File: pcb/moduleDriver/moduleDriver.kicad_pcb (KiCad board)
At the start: 2 copper layers, 70 x 80 mm, 37 parts, among them J1 MOTOR, J10 Sensor, J11 Power, J12 Power, J13 Power, J2 MOTOR, J3 MOTOR, J4 MOTOR, J5 IDC, J6 IDC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

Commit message: Simple PCB fixes
- Change C2, C3, C5, C6 all to 1uF
- Delete R4
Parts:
- C2, C3, C5, C6: value 0.1uF -> 1uF
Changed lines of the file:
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@@
       (effects (font (size 1 1) (thickness 0.15)))
     )
-    (fp_text value "0.1uF" (at 0 1.43) (layer "F.Fab")
+    (fp_text value "1uF" (at 0 1.43) (layer "F.Fab")
       (effects (font (size 1 1) (thickness 0.15)))
     )
@@
       (effects (font (size 1 1) (thickness 0.15)))
     )
-    (fp_text value "0.1uF" (at 0 1.43) (layer "F.Fab")
+    (fp_text value "1uF" (at 0 1.43) (layer "F.Fab")
       (effects (font (size 1 1) (thickness 0.15)))
     )
@@
       (effects (font (size 1 1) (thickness 0.15)))
     )
-    (fp_text value "0.1uF" (at 0 1.43 90) (layer "F.Fab")
+    (fp_text value "1uF" (at 0 1.43 90) (layer "F.Fab")
       (effects (font (size 1 1) (thickness 0.15)))
     )
@@
       (effects (font (size 1 1) (thickness 0.15)))
     )
-    (fp_text value "0.1uF" (at 0 1.43 90) (layer "F.Fab")
-      (effects (font (size 1 1) (thickness 0.15)))
-    )
+    (fp_text value "1uF" (at 0 1.43 90) (layer "F.Fab")
+      (effects (font (size 1 1) (thickness 0.15)))
+    )

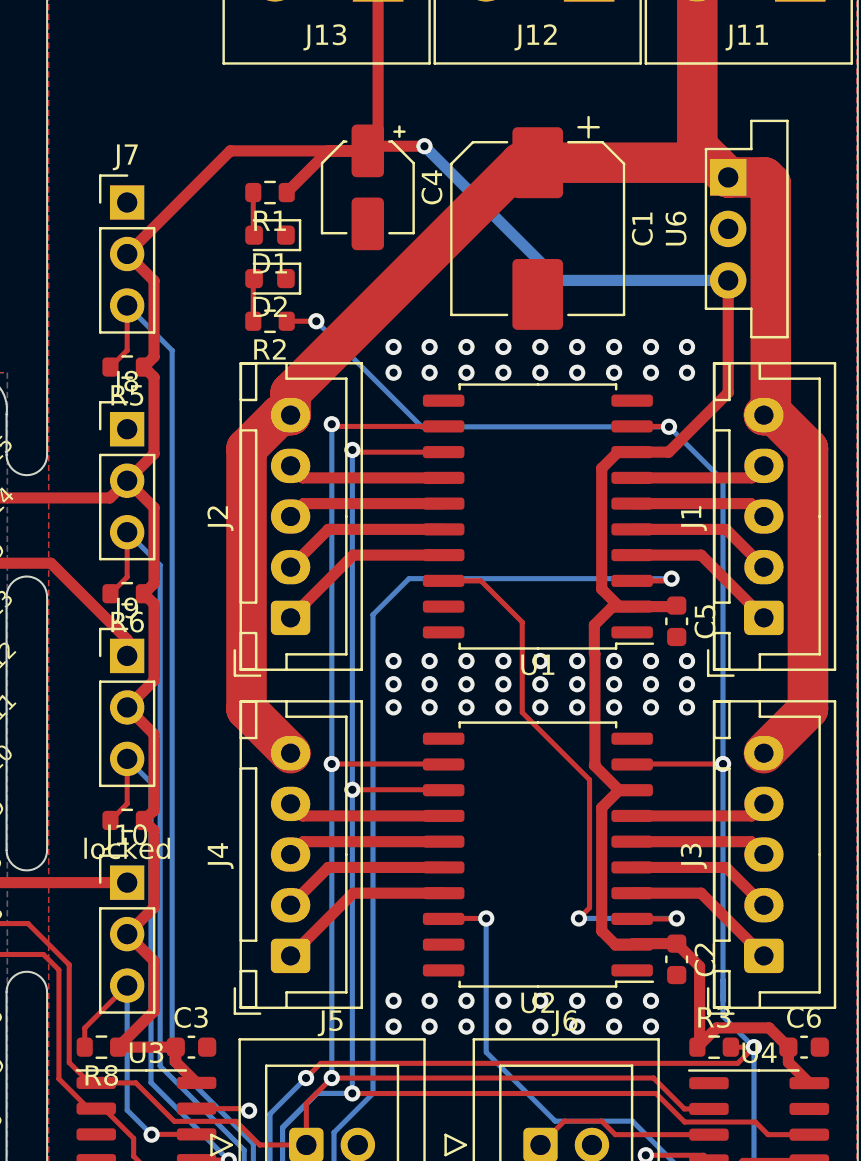
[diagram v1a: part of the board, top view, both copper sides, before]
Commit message: Added 12v led
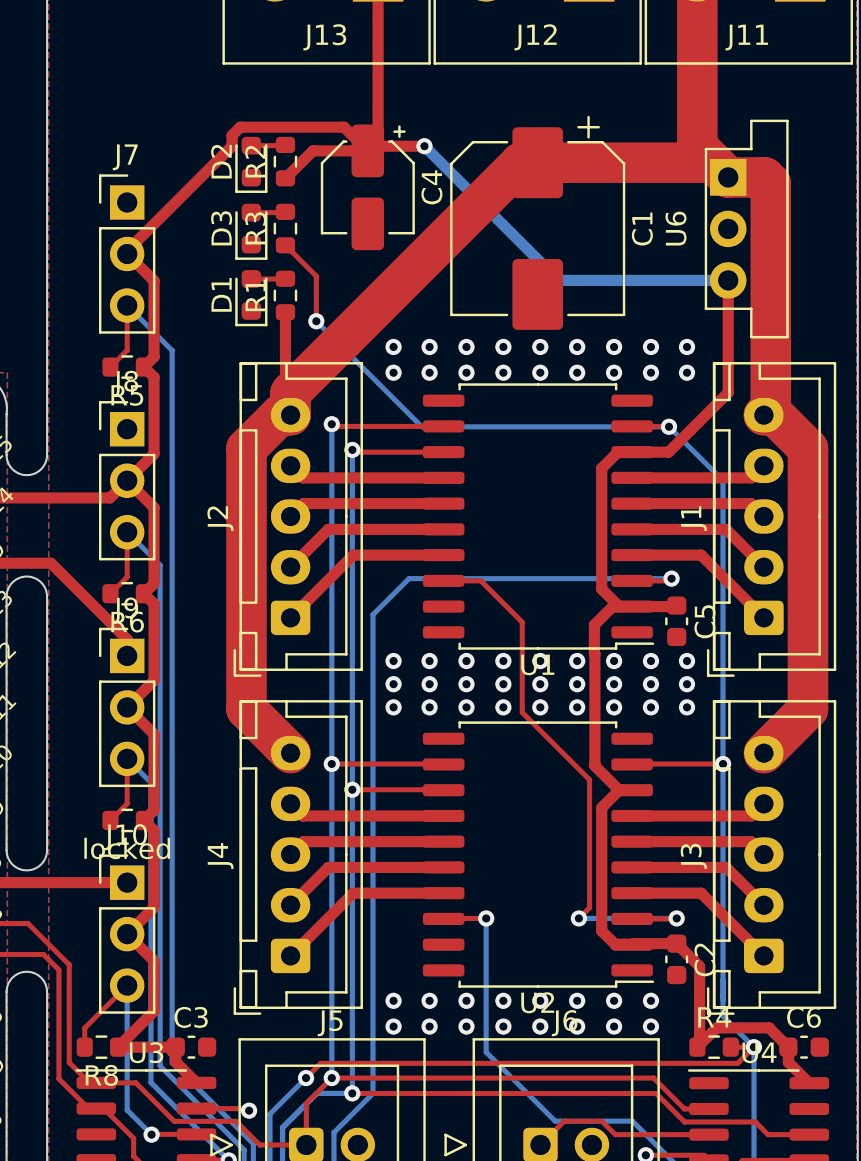
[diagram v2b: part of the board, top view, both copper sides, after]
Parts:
- added D1: LED, LED_SMD:LED_0603_1608Metric, F.Cu at (110.1, 72.1)
- added R1: 220R, Resistor_SMD:R_0603_1608Metric, F.Cu at (111.8, 72.1)
- moved R3 4.64 mm to (111.8, 68.8), turned to 90 degrees
- moved D2 3.74 mm to (110.1, 65.5), turned to 90 degrees
- moved D3 2.63 mm to (110.1, 68.8), turned to 90 degrees
- moved R2 1.70 mm to (111.8, 65.5), turned to 90 degrees
- renumbered D1 to D2, D2 to D3, R1 to R2, R2 to R3, R3 to R4
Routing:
- net +12V: track 94.7 -> 99.9 mm
- net /PWR_ENABLE_IN: track 125.8 -> 128.7 mm
- net Net-(D1-Pad2): track 0.00 -> 1.69 mm
- net +5V: track 248.5 -> 249.6 mm

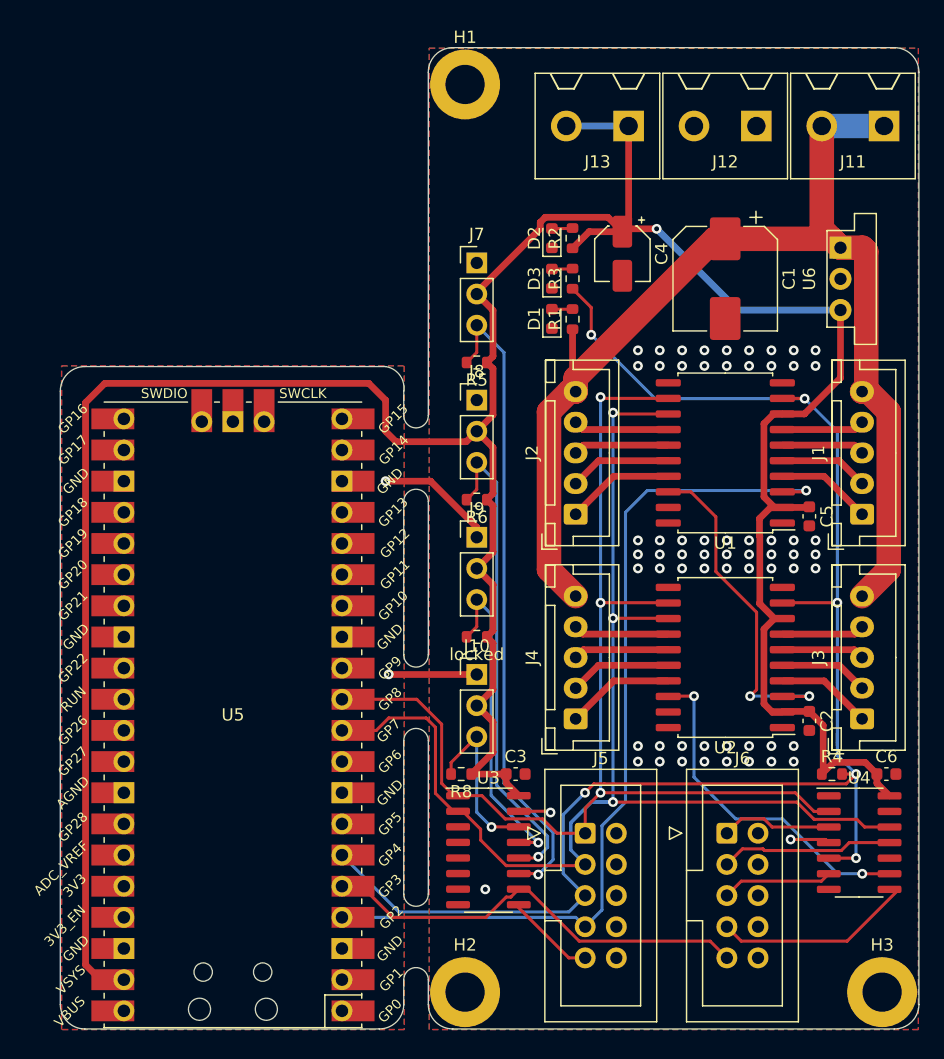
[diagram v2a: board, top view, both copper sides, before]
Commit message: Inital layout for voltage level translation
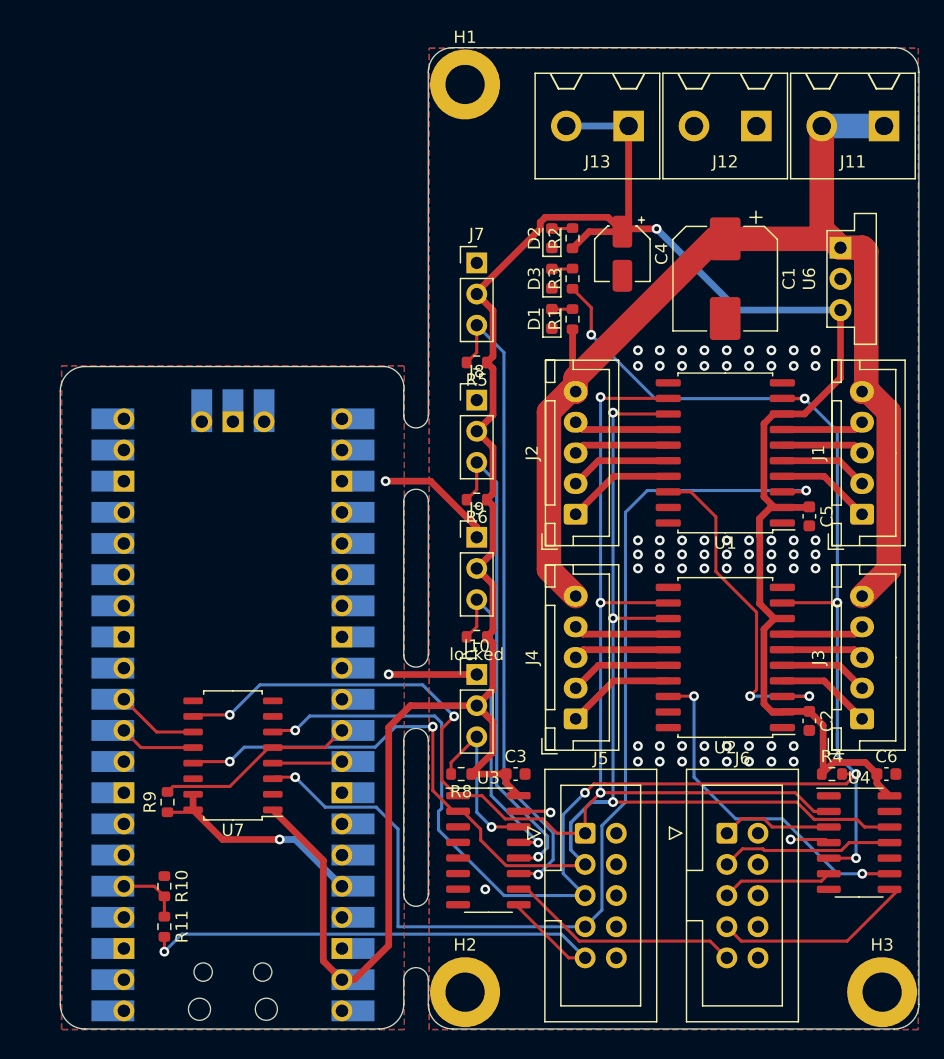
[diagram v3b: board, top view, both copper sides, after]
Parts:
- added R10: 2k, Resistor_SMD:R_0603_1608Metric, F.Cu at (78.5, 118.4)
- added R11: 1k, Resistor_SMD:R_0603_1608Metric, F.Cu at (78.5, 121.7)
- added R9: 5k, Resistor_SMD:R_0603_1608Metric, F.Cu at (78.7, 111.5)
- added U7: HEF4104B, Package_SO:SOIC-16_4.55x10.3mm_P1.27mm, F.Cu at (84.1, 107.7)
- U5: moved to B.Cu
- turned U5 to 0 degrees
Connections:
- U5 pad 10: /CLOCK_IN -> /CLOCK_IN_3V3
- U5 pad 11: /LATCH_IN -> /LATCH_IN_3V3
- U5 pad 31: unconnected-(U5-Pad31) -> /PWR_ENABLE_IN_3V3
- U5 pad 32: unconnected-(U5-Pad32) -> /MOTOR_IN_3V3
- U5 pad 36: unconnected-(U5-Pad36) -> +3.3V
- U5 pad 4: /MOTOR_IN -> unconnected-(U5-Pad4)
- U5 pad 5: /SENSOR_IN -> /SENSOR_OUT_3V3
- U5 pad 6: /PWR_ENABLE_IN -> unconnected-(U5-Pad6)
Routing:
- net +5V: track 249.6 -> 210.6 mm
- net /SENSOR_OUT: track 7.46 -> 44.4 mm, vias 0 -> 1
- net +3.3V: track 0.00 -> 18.2 mm, vias 0 -> 1
- net /SENSOR_IN: track 36.0 -> 19.5 mm
- net /PWR_ENABLE_IN_3V3: track 0.00 -> 16.3 mm
- net /LATCH_IN: track 93.6 -> 108.9 mm, vias 3 -> 5
- net /PWR_ENABLE_IN: track 128.7 -> 144.0 mm, vias 6 -> 7
- net /MOTOR_IN: track 72.7 -> 87.8 mm, vias 1 -> 2
- net /CLOCK_IN: track 107.5 -> 120.1 mm, vias 3 -> 5
- net /LATCH_IN_3V3: track 0.00 -> 6.74 mm
- net /CLOCK_IN_3V3: track 0.00 -> 6.22 mm
- net /MOTOR_IN_3V3: track 0.00 -> 5.69 mm
- net /SENSOR_OUT_3V3: track 0.00 -> 5.30 mm

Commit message: Rework pico layout
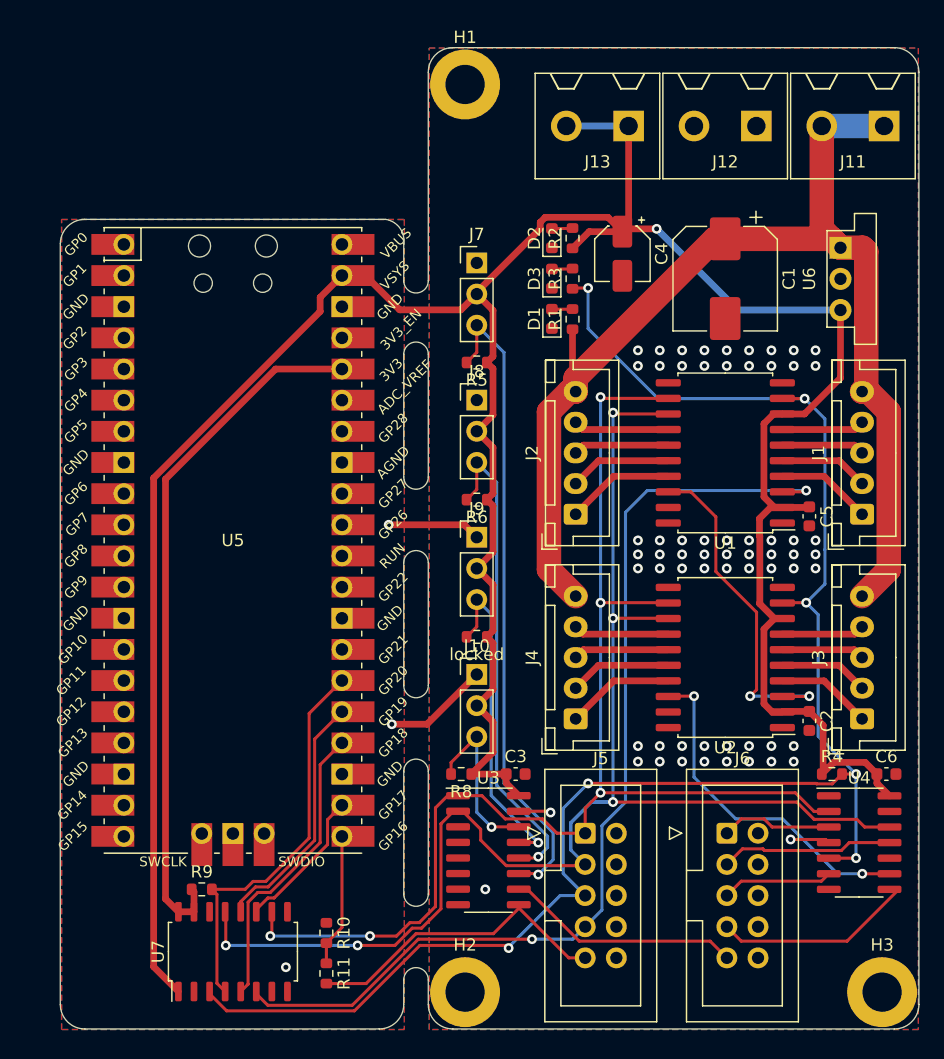
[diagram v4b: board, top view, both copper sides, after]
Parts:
- U5: moved to F.Cu
- moved U7 16.0 mm to (84.1, 123.7), turned to 90 degrees
- moved U5 14.2 mm to (84.1, 90.2)
- moved R10 13.7 mm to (91.7, 122.2)
- moved R11 13.7 mm to (91.7, 125.5)
- moved R9 7.64 mm to (81.5, 118.6), turned to 0 degrees
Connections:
- U5 pad 10: /CLOCK_IN_3V3 -> unconnected-(U5-Pad10)
- U5 pad 11: /LATCH_IN_3V3 -> unconnected-(U5-Pad11)
- U5 pad 21: unconnected-(U5-Pad21) -> /SENSOR_OUT_3V3
- U5 pad 22: unconnected-(U5-Pad22) -> /LATCH_IN_3V3
- U5 pad 24: unconnected-(U5-Pad24) -> /MOTOR_IN_3V3
- U5 pad 25: unconnected-(U5-Pad25) -> /CLOCK_IN_3V3
- U5 pad 26: unconnected-(U5-Pad26) -> /PWR_ENABLE_IN_3V3
- U5 pad 31: /PWR_ENABLE_IN_3V3 -> unconnected-(U5-Pad31)
- U5 pad 32: /MOTOR_IN_3V3 -> unconnected-(U5-Pad32)
- U5 pad 5: /SENSOR_OUT_3V3 -> unconnected-(U5-Pad5)
- U7 pad 3: /MOTOR_IN -> /PWR_ENABLE_IN
- U7 pad 4: /MOTOR_IN_3V3 -> /PWR_ENABLE_IN_3V3
- U7 pad 5: /PWR_ENABLE_IN_3V3 -> /MOTOR_IN_3V3
- U7 pad 6: /PWR_ENABLE_IN -> /MOTOR_IN
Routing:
- net +3.3V: track 18.2 -> 57.0 mm, vias 1 -> 0
- net +5V: track 210.6 -> 242.0 mm
- net /MOTOR_IN_3V3: track 5.69 -> 24.3 mm
- net /SENSOR_OUT: track 44.4 -> 26.0 mm, vias 1 -> 0
- net /PWR_ENABLE_IN_3V3: track 16.3 -> 32.4 mm
- net /CLOCK_IN_3V3: track 6.22 -> 20.3 mm
- net /SENSOR_OUT_3V3: track 5.30 -> 10.9 mm
- net /MOTOR_IN: track 87.8 -> 82.6 mm
- net /LATCH_IN_3V3: track 6.74 -> 11.9 mm
- net /PWR_ENABLE_IN: track 144.0 -> 139.5 mm
- net /LATCH_IN: track 108.9 -> 104.8 mm
- net /CLOCK_IN: track 120.1 -> 121.6 mm
- net GND: track 23.1 -> 22.3 mm, vias 66 -> 67
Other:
- outline, holes or cut-outs redrawn

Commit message: Reduce traces on ground plane
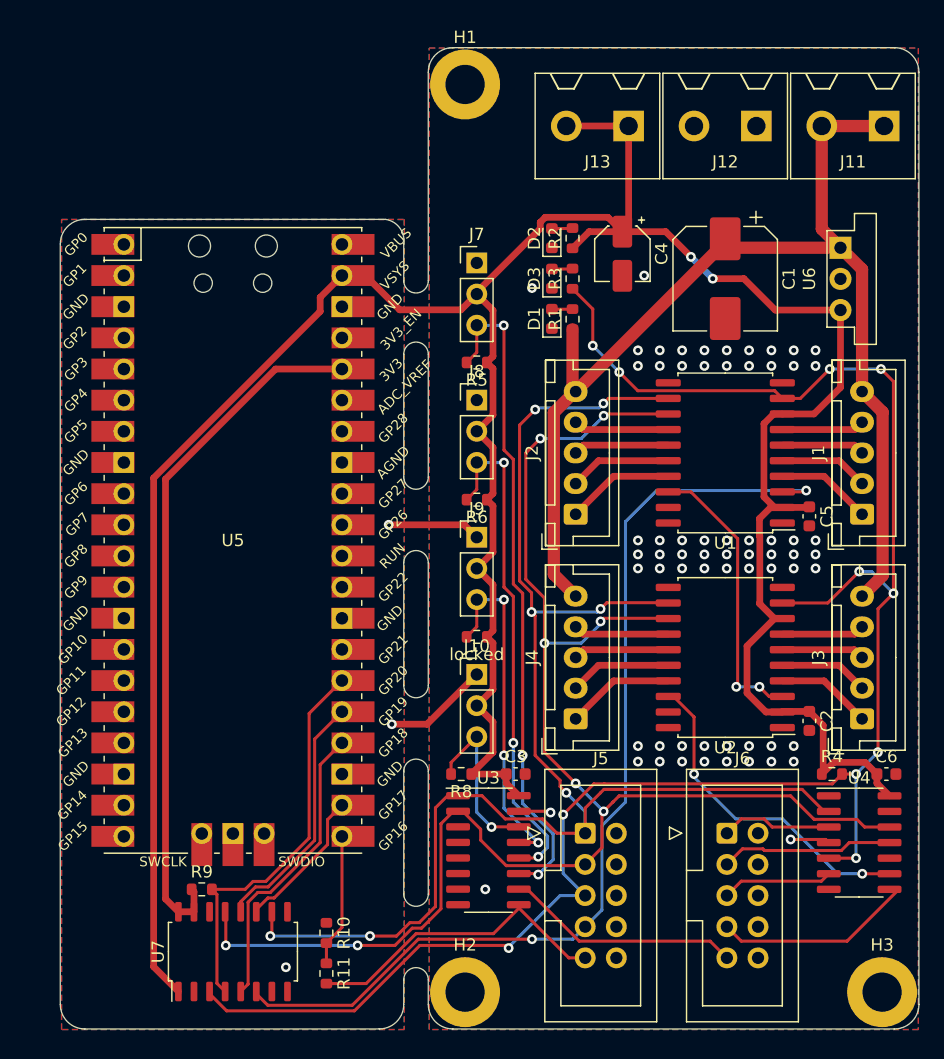
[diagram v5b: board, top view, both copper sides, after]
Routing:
- net /LATCH_IN: track 104.8 -> 121.7 mm, vias 5 -> 7
- net /PWR_ENABLE_IN: track 139.5 -> 154.3 mm, vias 7 -> 11
- net /CLOCK_IN: track 121.6 -> 128.7 mm, vias 5 -> 8
- net Net-(U1-Pad18): track 28.0 -> 23.4 mm
- net +12V: track 99.9 -> 96.7 mm
- net +5V: track 242.0 -> 243.7 mm, vias 1 -> 2
- net /MOTOR_SER_OUT: track 27.9 -> 26.5 mm
- net /SENSOR_C: track 27.1 -> 28.4 mm, vias 1 -> 3
- net /SENSOR_B: track 40.1 -> 41.4 mm, vias 1 -> 3
- net /SENSOR_A: track 52.9 -> 54.1 mm, vias 1 -> 3
- net GND: vias 67 -> 69

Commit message: Reduce traces on ground plane
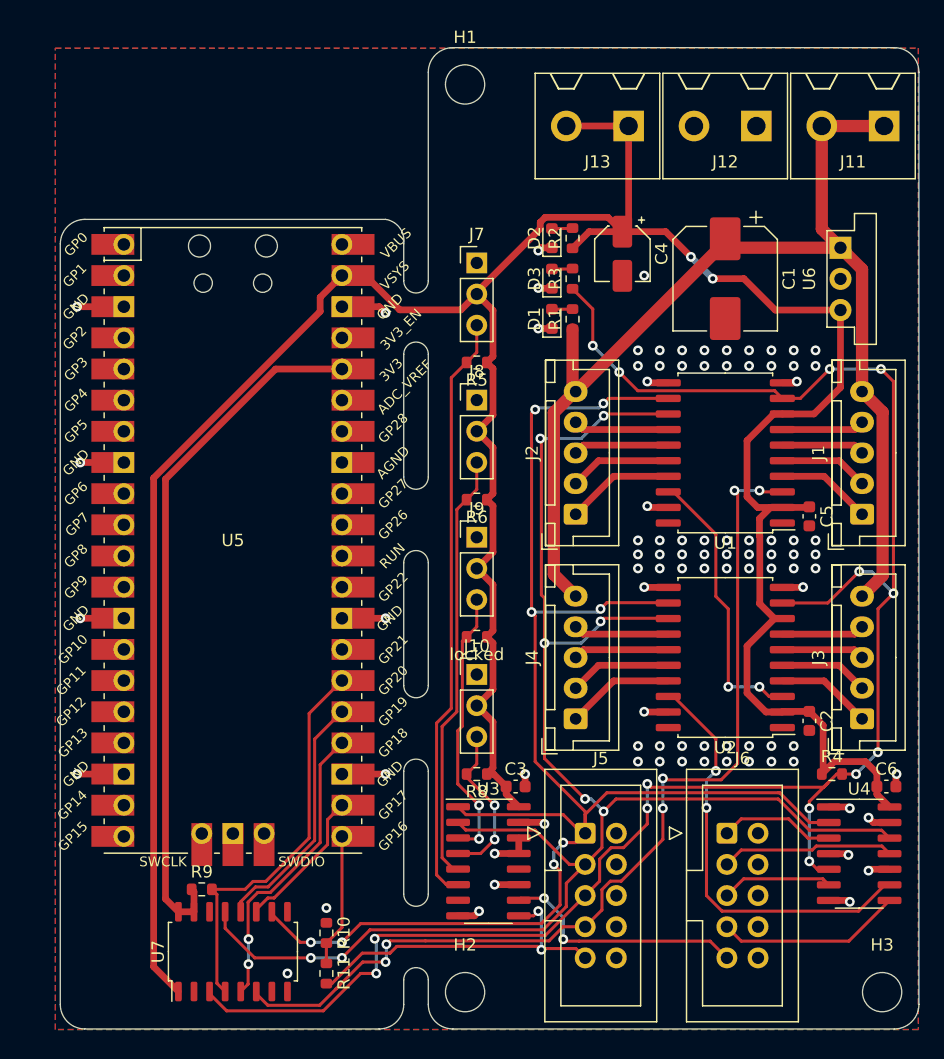
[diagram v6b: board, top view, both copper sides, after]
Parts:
- H1, H2, H3: footprint MountingHole:MountingHole_3.2mm_M3_ISO7380_Pad -> MountingHole:MountingHole_3.2mm_M3_ISO7380
- moved R8 1.27 mm to (104.0, 109.2)
- moved C3 1.02 mm to (107.1, 110.2)
- moved C6 1.02 mm to (137.3, 110.2)
- moved U3 0.90 mm to (104.9, 116.3)
- moved U4 0.90 mm to (135.1, 115.7)
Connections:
- U3 pad 11: /SENSOR_A -> GND
- U3 pad 12: /SENSOR_B -> GND
- U3 pad 13: /SENSOR_C -> GND
- U3 pad 14: /SENSOR_D -> GND
- U3 pad 3: unconnected-(U3-Pad3) -> /SENSOR_C
- U3 pad 4: unconnected-(U3-Pad4) -> /SENSOR_D
- U3 pad 5: unconnected-(U3-Pad5) -> /SENSOR_B
- U3 pad 6: unconnected-(U3-Pad6) -> /SENSOR_A
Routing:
- net GND: track 22.3 -> 59.7 mm, vias 69 -> 91
- net /MOTOR_SER_OUT: track 26.5 -> 34.3 mm
- net /SENSOR_B: track 41.4 -> 35.1 mm, vias 3 -> 0
- net /SENSOR_A: track 54.1 -> 48.2 mm, vias 3 -> 0
- net /SENSOR_C: track 28.4 -> 22.6 mm, vias 3 -> 2
- net /LATCH_IN: track 121.7 -> 127.2 mm, vias 7 -> 8
- net /CLOCK_IN: track 128.7 -> 132.9 mm
- net /MOTOR_IN: track 82.2 -> 79.1 mm, vias 2 -> 6
- net /SENSOR_OUT: track 26.0 -> 27.8 mm, vias 0 -> 2
- net /PWR_ENABLE_IN: track 154.3 -> 152.5 mm, vias 11 -> 14
- net +5V: track 243.7 -> 245.2 mm
- net /MOTOR_OUT: track 16.3 -> 15.1 mm
- net /SENSOR_D: track 14.0 -> 13.1 mm, vias 1 -> 2
- net /SENSOR_IN: track 19.5 -> 20.1 mm, vias 0 -> 2
- net Net-(U1-Pad18): track 23.4 -> 22.9 mm
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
